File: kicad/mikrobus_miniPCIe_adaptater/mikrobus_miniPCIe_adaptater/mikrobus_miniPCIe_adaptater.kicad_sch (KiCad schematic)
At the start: 2 parts, among them IC101 MIKROE-924, J101 Bus_PCI_Express_Mini

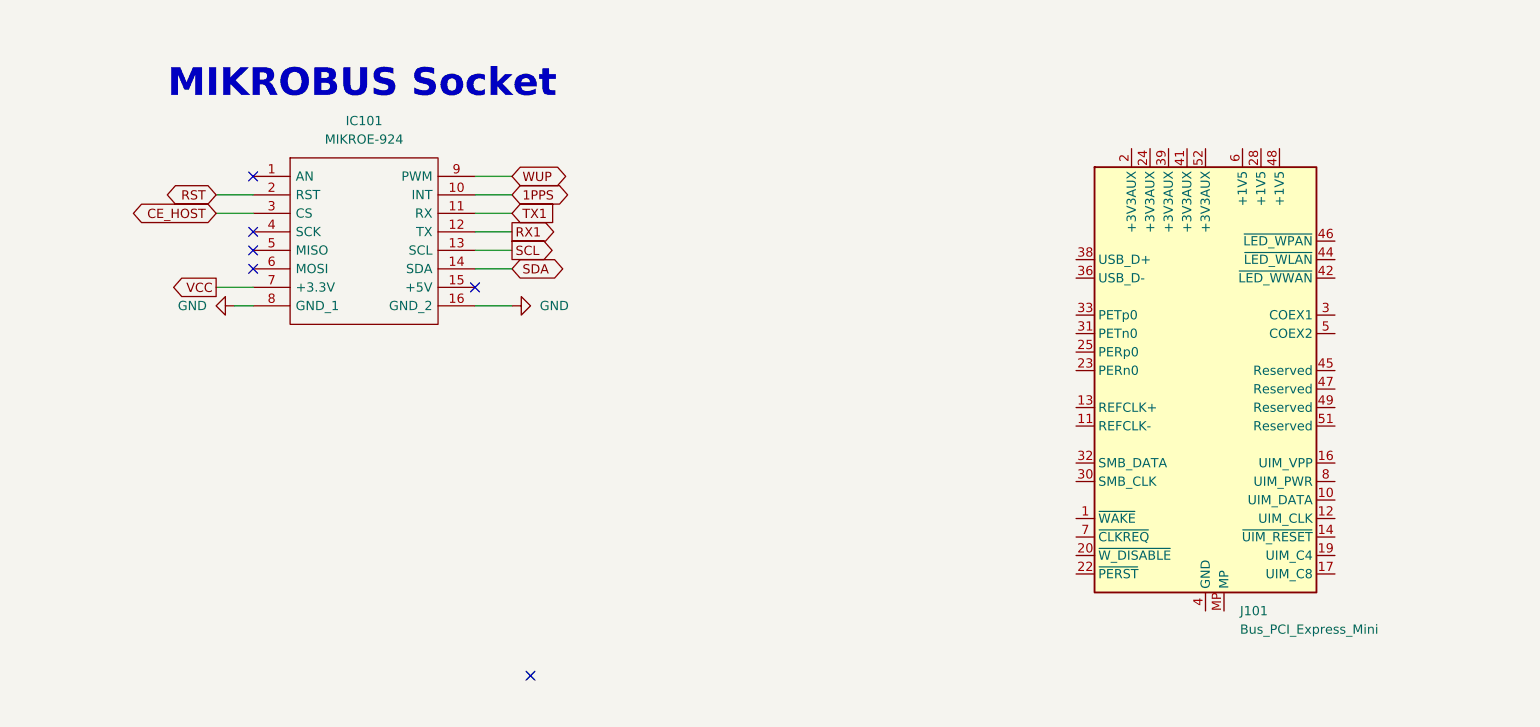
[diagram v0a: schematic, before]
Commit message: add power and gnd
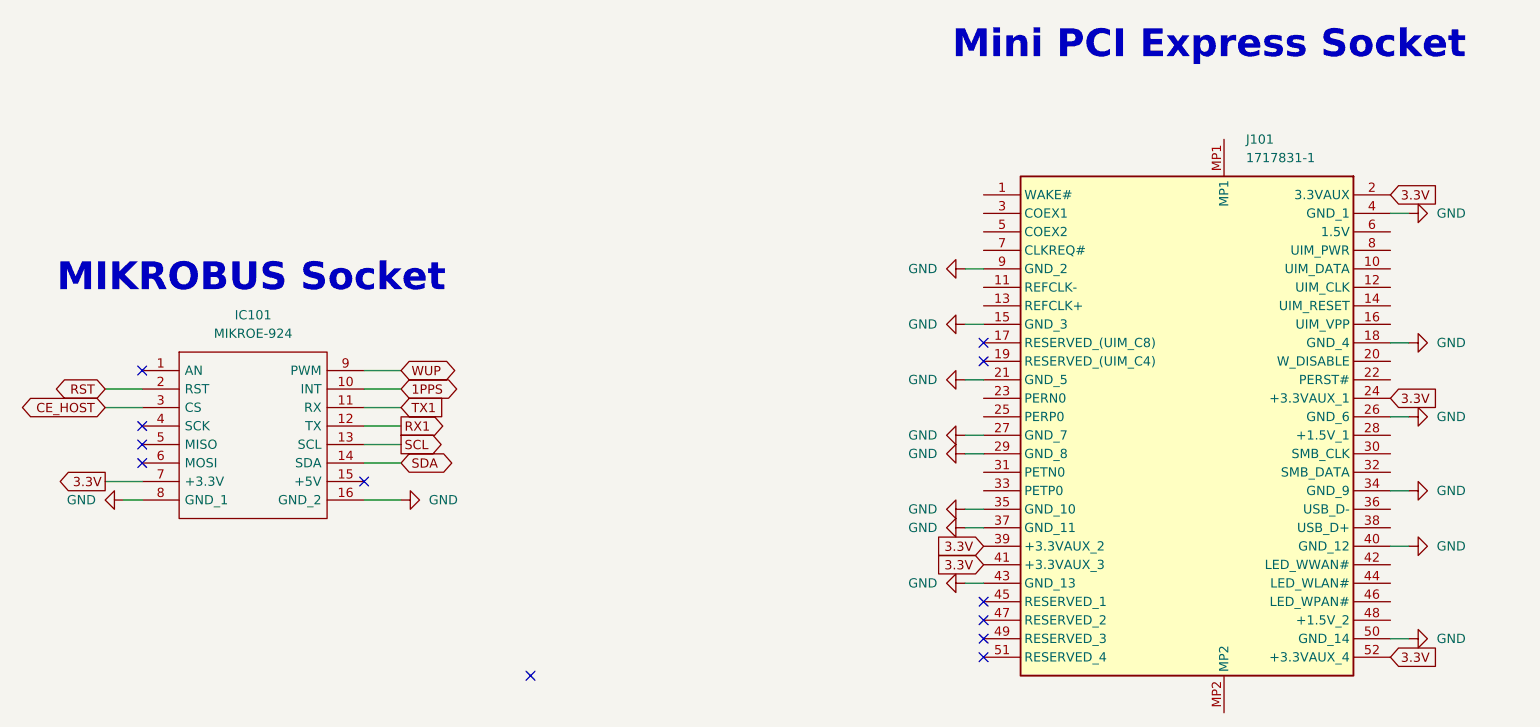
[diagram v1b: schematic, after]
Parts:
- removed J101: Bus_PCI_Express_Mini, Connector_PCBEdge:BUS_PCI_Express_Mini, symbol Connector:Bus_PCI_Express_Mini
- added J101: 1717831-1, 17178311, symbol Mini_PCI_e:1717831-1
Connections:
- net GND: now also J101.15 (GND_3), J101.18 (GND_4), J101.21 (GND_5), J101.26 (GND_6), J101.27 (GND_7), J101.29 (GND_8), J101.34 (GND_9), J101.35 (GND_10), J101.37 (GND_11), J101.4 (GND_1), J101.40 (GND_12), J101.43 (GND_13), J101.50 (GND_14), J101.9 (GND_2)
- net VCC renamed 3.3V
- net 3.3V: now also J101.2 (3.3VAUX), J101.24 (+3.3VAUX_1), J101.39 (+3.3VAUX_2), J101.41 (+3.3VAUX_3), J101.52 (+3.3VAUX_4)
- no-connect marks 6 -> 12
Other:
- note added: "Mini PCI Express Socket"
- moved on the sheet: IC101
